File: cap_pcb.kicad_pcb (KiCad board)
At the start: 2 copper layers, 100 x 81 mm, 41 parts, among them J1 Conn_02x09_Odd_Even, J10 Expansion Board, J11 Aux_mio_conn, J12 12v Pwr, J13 HDMI_A, J14 PL Pins, J15 Conn_02x06 Extension, J16 Conn_01x02_Pin, J17 SD_MODULE_CONN, J18 EMMC_CONN, J2 Conn_02x09_Odd_Even, J3 Conn_02x09_Odd_Even, J4 Conn_02x09_Odd_Even, J5 Conn_02x09_Odd_Even, J6 Conn_02x09_Odd_Even, J7 Conn_02x09_Odd_Even, J8 Conn_02x09_Odd_Even, J9 Conn_02x09_Odd_Even, U1 L7805, U3 TPS5430DDA

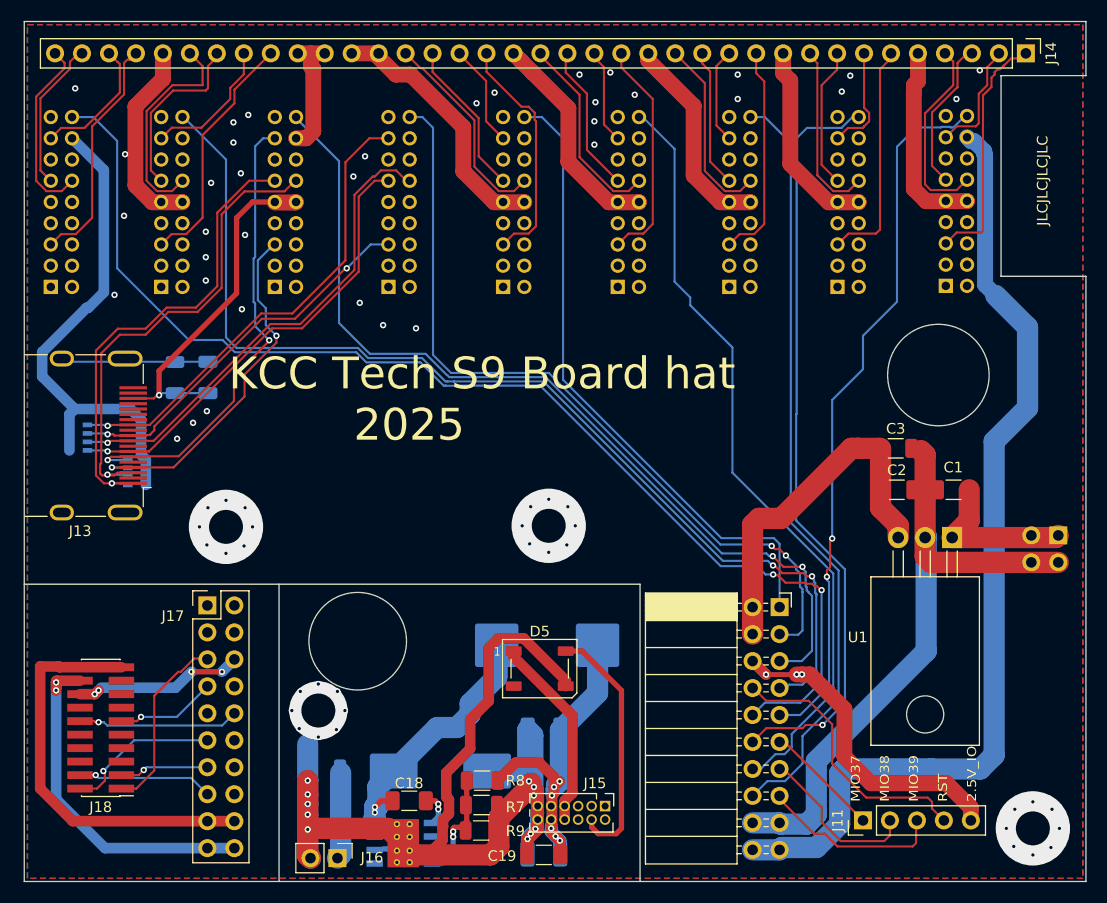
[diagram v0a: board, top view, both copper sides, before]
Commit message: - Added capacitors on HDMI TDMS lines
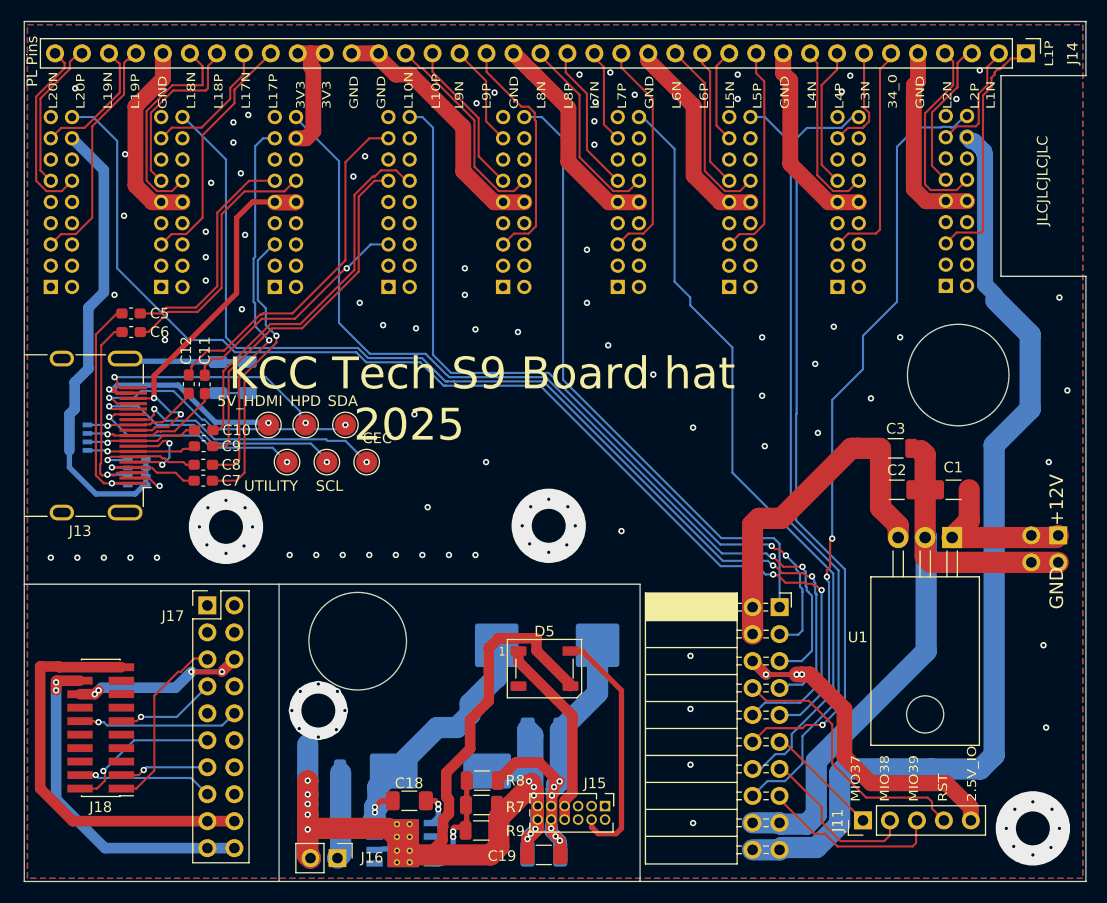
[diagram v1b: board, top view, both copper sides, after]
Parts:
- added C10: 100n, Capacitor_SMD:C_0603_1608Metric_Pad1.08x0.95mm_HandSolder, F.Cu at (41.9, 79.5)
- added C11: 100n, Capacitor_SMD:C_0603_1608Metric_Pad1.08x0.95mm_HandSolder, F.Cu at (42.0, 75.2)
- added C12: 100n, Capacitor_SMD:C_0603_1608Metric_Pad1.08x0.95mm_HandSolder, F.Cu at (40.5, 75.2)
- added C5: 100n, Capacitor_SMD:C_0603_1608Metric_Pad1.08x0.95mm_HandSolder, F.Cu at (35.1, 68.5)
- added C6: 100n, Capacitor_SMD:C_0603_1608Metric_Pad1.08x0.95mm_HandSolder, F.Cu at (35.1, 70.2)
- added C7: 100n, Capacitor_SMD:C_0603_1608Metric_Pad1.08x0.95mm_HandSolder, F.Cu at (41.9, 84.2)
- added C8: 100n, Capacitor_SMD:C_0603_1608Metric_Pad1.08x0.95mm_HandSolder, F.Cu at (41.9, 82.8)
- added C9: 100n, Capacitor_SMD:C_0603_1608Metric_Pad1.08x0.95mm_HandSolder, F.Cu at (41.9, 81.0)
- added TP1: CEC, TestPoint:TestPoint_Pad_D2.0mm, F.Cu at (57.2, 82.5)
- added TP2: SCL, TestPoint:TestPoint_Pad_D2.0mm, F.Cu at (53.5, 82.5)
- added TP3: SDA, TestPoint:TestPoint_Pad_D2.0mm, F.Cu at (55.2, 79.0)
- added TP4: HPD, TestPoint:TestPoint_Pad_D2.0mm, F.Cu at (51.5, 79.0)
- added TP5: UTILITY, TestPoint:TestPoint_Pad_D2.0mm, F.Cu at (49.8, 82.5)
- added TP6: 5V_HDMI, TestPoint:TestPoint_Pad_D2.0mm, F.Cu at (48.0, 79.0)
- J10: value Expansion Board -> USB Expansion board
- moved R1 4.05 mm to (43.2, 74.5)
- moved C4 3.70 mm to (46.0, 74.5)
- moved D5 0.45 mm to (74.0, 102.0)
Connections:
- net /+VIN renamed /Modules/+VIN
- net /SD_D0 renamed /Modules/SD_D0
- net /SD_D1 renamed /Modules/SD_D1
- net /SD_D2 renamed /Modules/SD_D2
- net /SD_D3 renamed /Modules/SD_D3
- net /SD­_3.3V renamed /Modules/SD­_3.3V
- net /SD­_CLK renamed /Modules/SD­_CLK
- net /SD­_VCC_IO renamed /Modules/SD­_VCC_IO
- net /SD­­_CMD renamed /Modules/SD­­_CMD
- J13 pad 1: /BANK34_L16P_TXD7 -> Net-(J13-D2+)
- J13 pad 10: /BANK34_L11P_PLUG6 -> Net-(J13-CK+)
- J13 pad 11: unconnected-(J13-CKS-Pad11) -> GND
- J13 pad 12: /BANK34_L11N_RST6 -> Net-(J13-CK-)
- J13 pad 13: unconnected-(J13-CEC-Pad13) -> Net-(J13-CEC)
- J13 pad 14: unconnected-(J13-UTILITY-Pad14) -> Net-(J13-UTILITY)
- J13 pad 15: unconnected-(J13-SCL-Pad15) -> Net-(J13-SCL)
- J13 pad 16: unconnected-(J13-SDA-Pad16) -> Net-(J13-SDA)
- J13 pad 18: unconnected-(J13-+5V-Pad18) -> Net-(J13-+5V)
- J13 pad 19: unconnected-(J13-HPD-Pad19) -> Net-(J13-HPD)
- J13 pad 2: unconnected-(J13-D2S-Pad2) -> GND
- J13 pad 3: /BANK34_L16N_RXD7 -> Net-(J13-D2-)
- J13 pad 4: /BANK34_L15P__PLUG7 -> Net-(J13-D1+)
- J13 pad 5: unconnected-(J13-D1S-Pad5) -> GND
- J13 pad 6: /BANK34_L15N_RST7 -> Net-(J13-D1-)
- J13 pad 7: /BANK34_L12P_TXD6 -> Net-(J13-D0+)
- J13 pad 8: unconnected-(J13-D0S-Pad8) -> GND
- J13 pad 9: /BANK34_L12N_RXD6 -> Net-(J13-D0-)
- J2 pad 16: /3.3V -> unconnected-(J2-Pin_16-Pad16)
- RN1 pad 1: /BANK34_L16P_TXD7 -> Net-(J13-D2+)
- RN1 pad 2: /BANK34_L16N_RXD7 -> Net-(J13-D2-)
- RN1 pad 3: /BANK34_L15P__PLUG7 -> Net-(J13-D1+)
- RN1 pad 4: /BANK34_L15N_RST7 -> Net-(J13-D1-)
- RN2 pad 1: /BANK34_L11N_RST6 -> Net-(J13-CK-)
- RN2 pad 2: /BANK34_L11P_PLUG6 -> Net-(J13-CK+)
- RN2 pad 3: /BANK34_L12N_RXD6 -> Net-(J13-D0-)
- RN2 pad 4: /BANK34_L12P_TXD6 -> Net-(J13-D0+)
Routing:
- net Net-(J13-SDA): track 0.00 -> 26.7 mm, vias 0 -> 2
- net Net-(J13-SCL): track 0.00 -> 25.2 mm, vias 0 -> 2
- net Net-(J13-CEC): track 0.00 -> 24.8 mm, vias 0 -> 2
- net /BANK34_L16P_TXD7: track 44.6 -> 21.8 mm, vias 1 -> 0
- net Net-(J13-HPD): track 0.00 -> 22.6 mm, vias 0 -> 2
- net Net-(J13-D2+): track 0.00 -> 21.9 mm, vias 0 -> 1
- net /BANK34_L16N_RXD7: track 45.7 -> 24.5 mm, vias 1 -> 0
- net Net-(J13-UTILITY): track 0.00 -> 20.9 mm, vias 0 -> 2
- net Net-(J13-D2-): track 0.00 -> 20.4 mm, vias 0 -> 1
- net GND: track 360.4 -> 379.5 mm, vias 84 -> 129
- net Net-(J13-+5V): track 0.00 -> 19.1 mm, vias 0 -> 2
- net Net-(J13-CK+): track 0.00 -> 12.6 mm, vias 0 -> 1
- net /BANK34_L11P_PLUG6: track 34.8 -> 23.1 mm, vias 2 -> 1
- net /BANK34_L11N_RST6: track 44.7 -> 33.5 mm, vias 1 -> 0
- net Net-(J13-D0-): track 0.00 -> 10.6 mm, vias 0 -> 1
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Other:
- outline, holes or cut-outs redrawn
- board text added: "3V3 GND GND L10N L10P"
- board text added: "GND +12V"
- board text added: "L18N L18P L17N L17P 3V3"
- board text added: "L1N"
- board text added: "L1P"
- board text added: "L20N L20P L19N L19P GND"
- board text added: "L3N 34_0 GND L2N L2P"
- board text added: "L5N L5P GND L4N L4P"
- board text added: "L7N L7P GND L6N L6P"
- board text added: "L9N L9P GND L8N L8P"
